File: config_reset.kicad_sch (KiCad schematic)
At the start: 20 parts, among them U1 NX1H35 PBGA625, U6 M95P32-IXMNT/E, Y2 LFSPXO025225_25MHz

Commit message: SDRAM, bank5
last iteration of sdram. max optimization routing and space wise. Traced 2 frams to Bank 5. Fanout of bank 5 for DF9
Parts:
- R1, R14, R19, R3, R31, R32, R6, R7, R8, R9: footprint Resistor_SMD:R_0603_1608Metric_Pad0.98x0.95mm_HandSolder -> Resistor_SMD:R_0402_1005Metric_Pad0.72x0.64mm_HandSolder
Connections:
- no-connect marks 21 -> 94

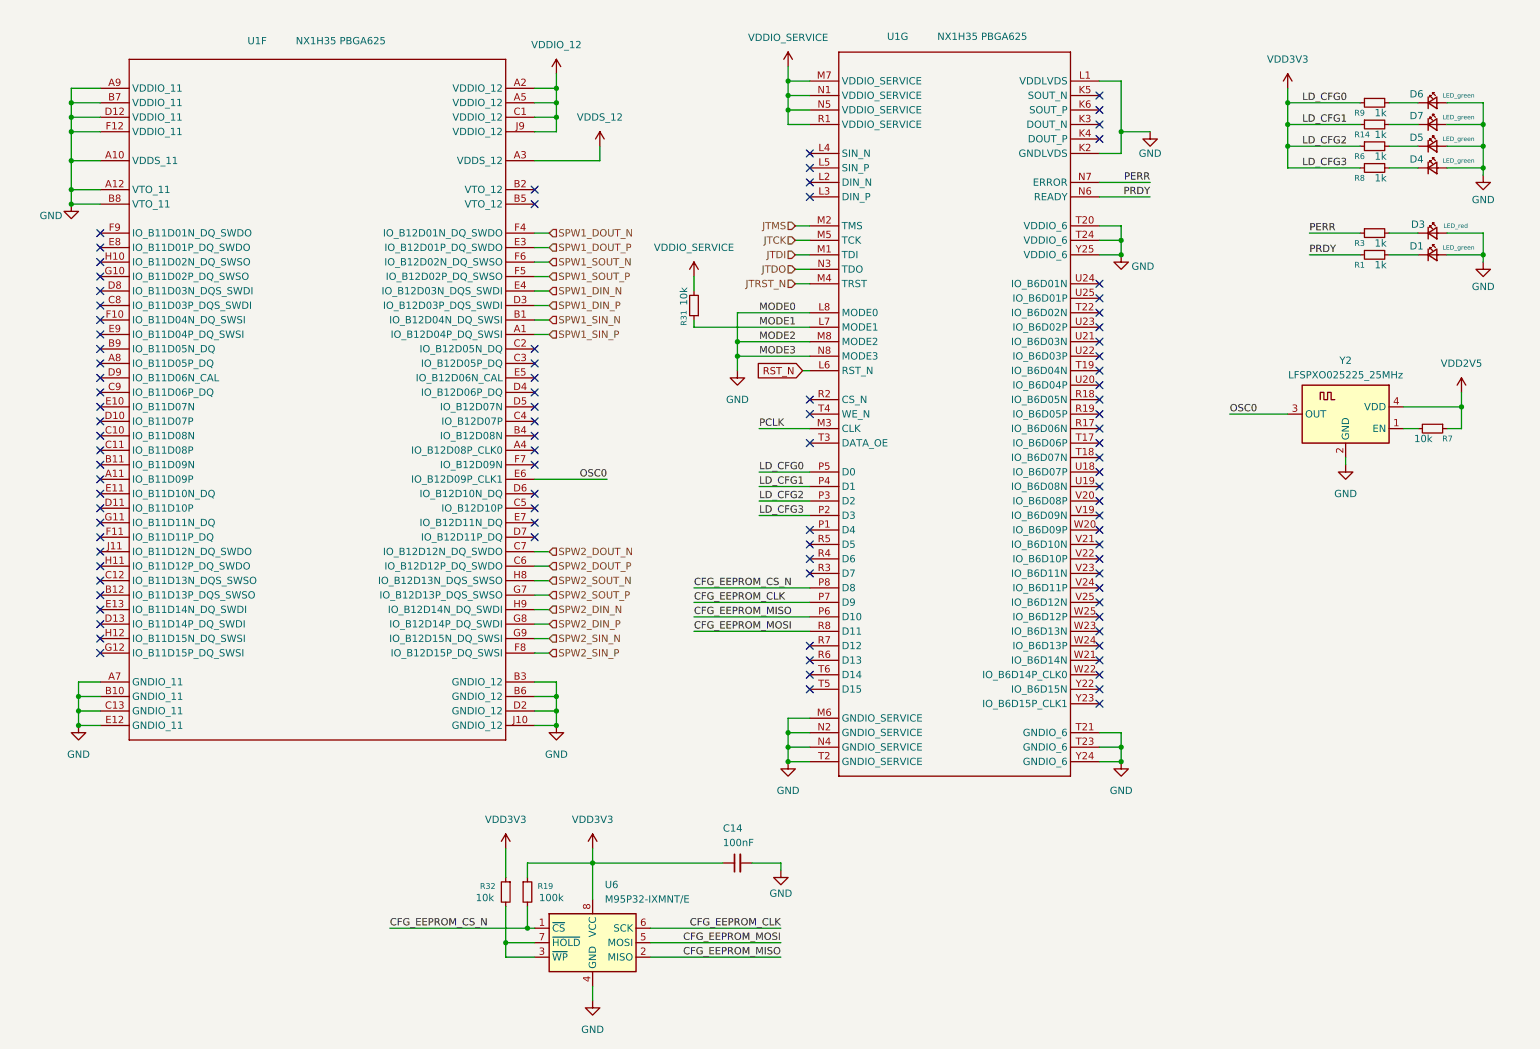
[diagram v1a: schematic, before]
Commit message: added MAX, picoblade, NPN
added the LDO (placement), added the picoblade connector for CFG and deleted one SPW out of 2 in the DF9.
added the NPN transistor (placed)
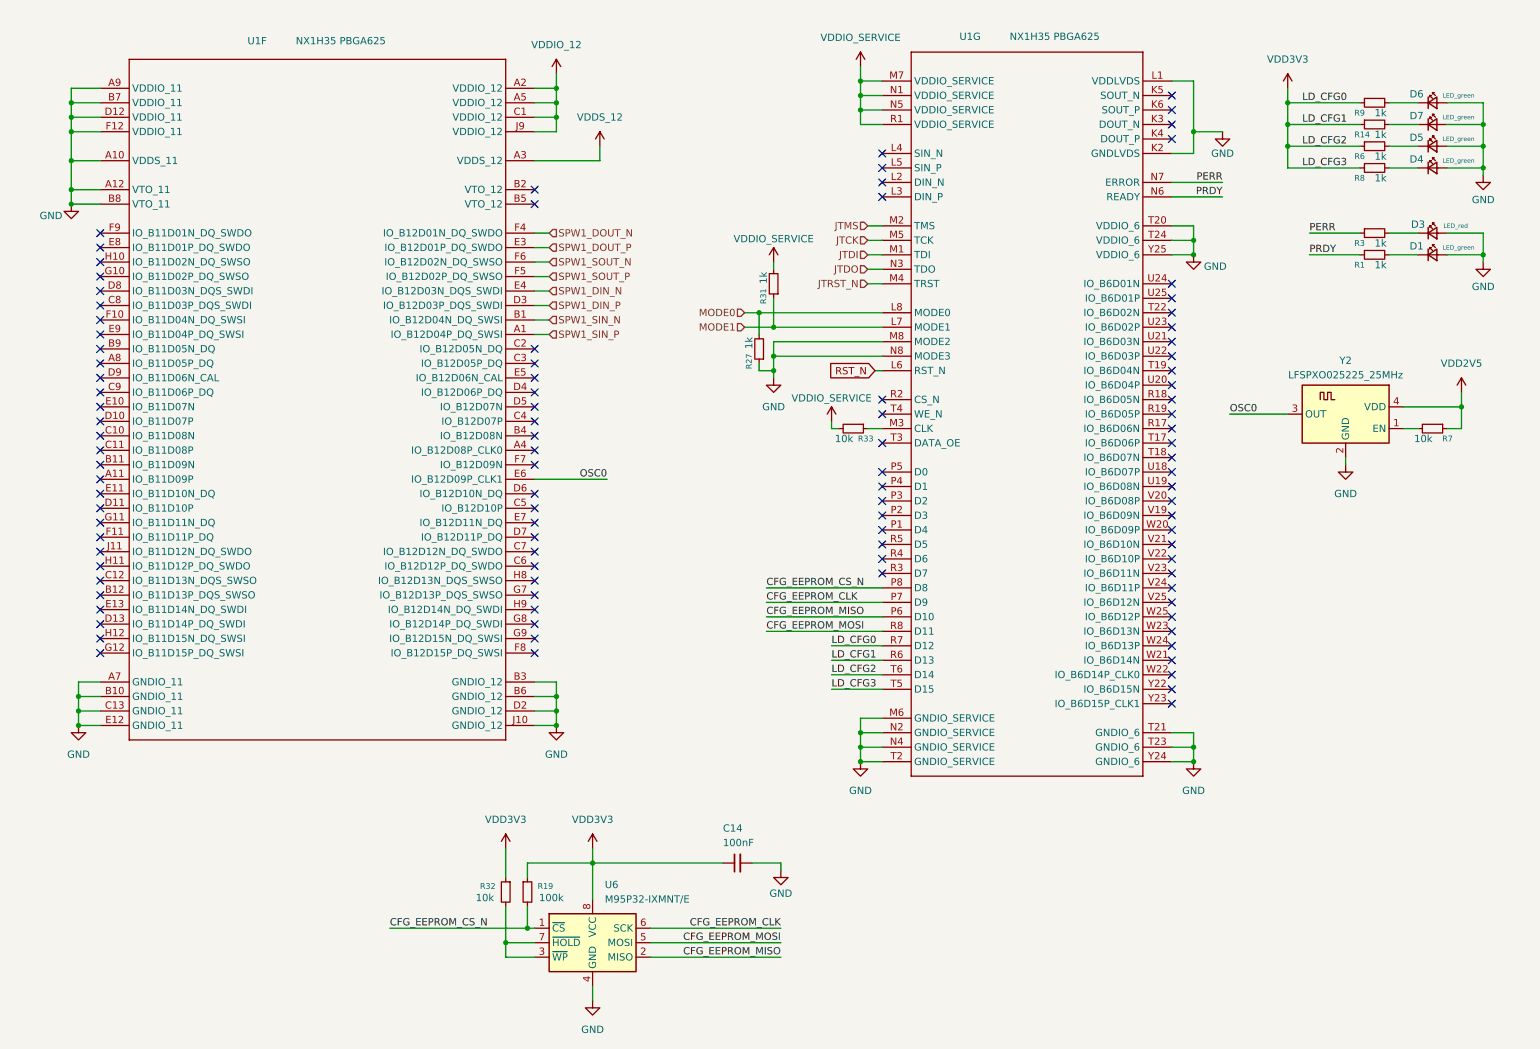
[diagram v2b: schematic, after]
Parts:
- added R27: 1k, Resistor_SMD:R_0402_1005Metric_Pad0.72x0.64mm_HandSolder, symbol Device:R_Small
- added R33: 10k, Resistor_SMD:R_0402_1005Metric_Pad0.72x0.64mm_HandSolder, symbol Device:R_Small
- R31: value 10k -> 1k
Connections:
- net GND: now also R27.1; no longer U1.L8 (MODE0)
- net VDD3V3: now also U1.R6 (D13), U1.R7 (D12), U1.T5 (D15), U1.T6 (D14); no longer U1.P2 (D3), U1.P3 (D2), U1.P4 (D1), U1.P5 (D0)
- net VDDIO_SERVICE: now also R33.2
- net PCLK: no longer names the net of U1.M3 (CLK)
- net PCLK: now also R33.1
- net SPW2_DIN_N: no longer names the net of U1.H9 (IO_B12D14N_DQ_SWDI)
- net SPW2_DIN_P: no longer names the net of U1.G8 (IO_B12D14P_DQ_SWDI)
- net SPW2_DOUT_N: no longer names the net of U1.C7 (IO_B12D12N_DQ_SWDO)
- net SPW2_DOUT_P: no longer names the net of U1.C6 (IO_B12D12P_DQ_SWDO)
- net SPW2_SIN_N: no longer names the net of U1.G9 (IO_B12D15N_DQ_SWSI)
- net SPW2_SIN_P: no longer names the net of U1.F8 (IO_B12D15P_DQ_SWSI)
- net SPW2_SOUT_N: no longer names the net of U1.H8 (IO_B12D13N_DQS_SWSO)
- net SPW2_SOUT_P: no longer names the net of U1.G7 (IO_B12D13P_DQS_SWSO)
- new net MODE0: R27.2, U1.L8 (MODE0)
- no-connect marks 94 -> 102
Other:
- moved on the sheet: U1G

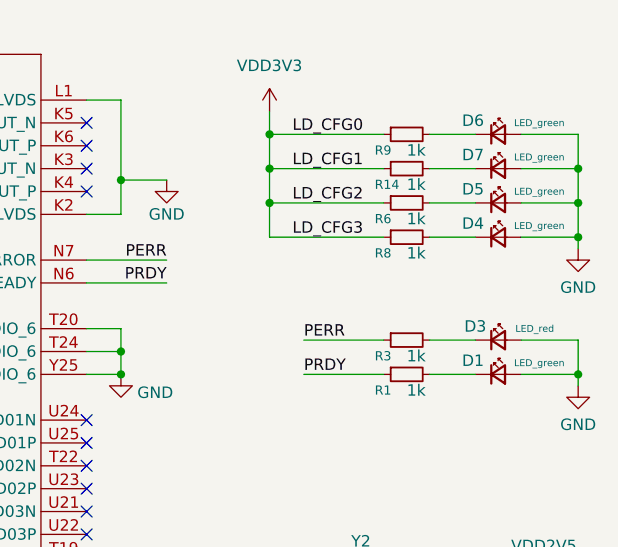
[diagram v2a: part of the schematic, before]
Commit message: full components, LEDS, changed edges
all components on pcb editor. added and  routed leds and 2 PLL. changed edges o have more space
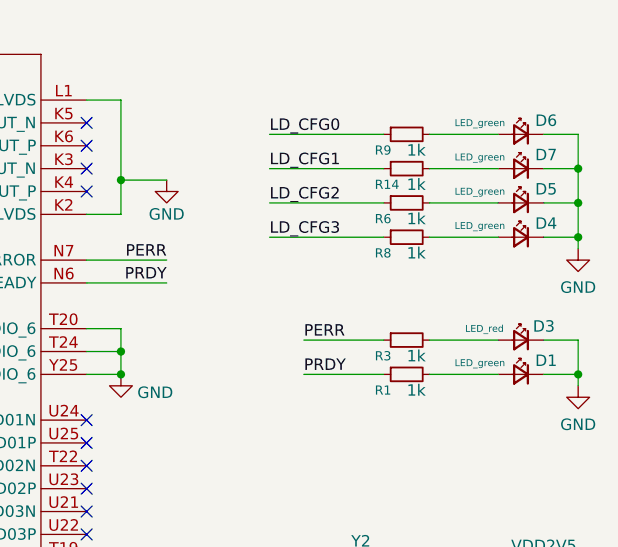
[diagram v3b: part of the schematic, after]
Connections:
- net GND: now also D1.1 (K), D3.1 (K), D4.1 (K), D5.1 (K), D6.1 (K), D7.1 (K); no longer D1.2 (A), D3.2 (A), D4.2 (A), D5.2 (A), D6.2 (A), D7.2 (A)
- net VDD3V3: no longer R14.1, R6.1, R8.1, R9.1, U1.R6 (D13), U1.R7 (D12), U1.T5 (D15), U1.T6 (D14)
- net at R6.2: now also D5.2 (A); no longer D5.1 (K)
- net at R8.2: now also D4.2 (A); no longer D4.1 (K)
- net at R9.2: now also D6.2 (A); no longer D6.1 (K)
- net at R1.2: now also D1.2 (A); no longer D1.1 (K)
- net at R14.2: now also D7.2 (A); no longer D7.1 (K)
- net at R3.2: now also D3.2 (A); no longer D3.1 (K)
- new net LD_CFG0: R9.1, U1.R7 (D12)
- new net LD_CFG1: R14.1, U1.R6 (D13)
- new net LD_CFG2: R6.1, U1.T6 (D14)
- new net LD_CFG3: R8.1, U1.T5 (D15)
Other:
- moved on the sheet: D1, D3, D4, D5, D6, D7

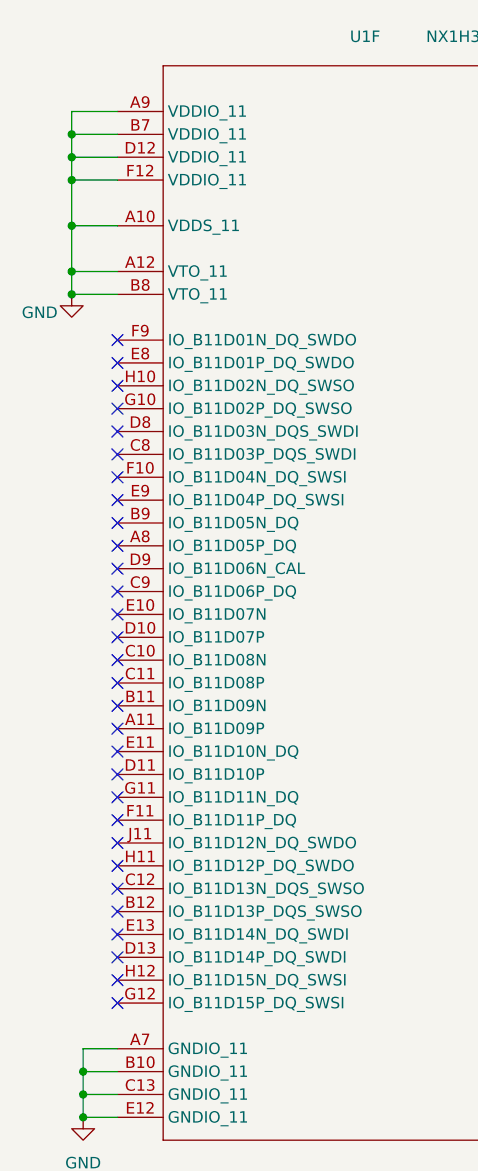
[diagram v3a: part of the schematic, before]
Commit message: SPW Bank0
completed SPW, rotated edges and adjusted dimensions to make the extra sdram bga fit. completed Bank 0 (still to route to connector). Started fanout of bga sdram
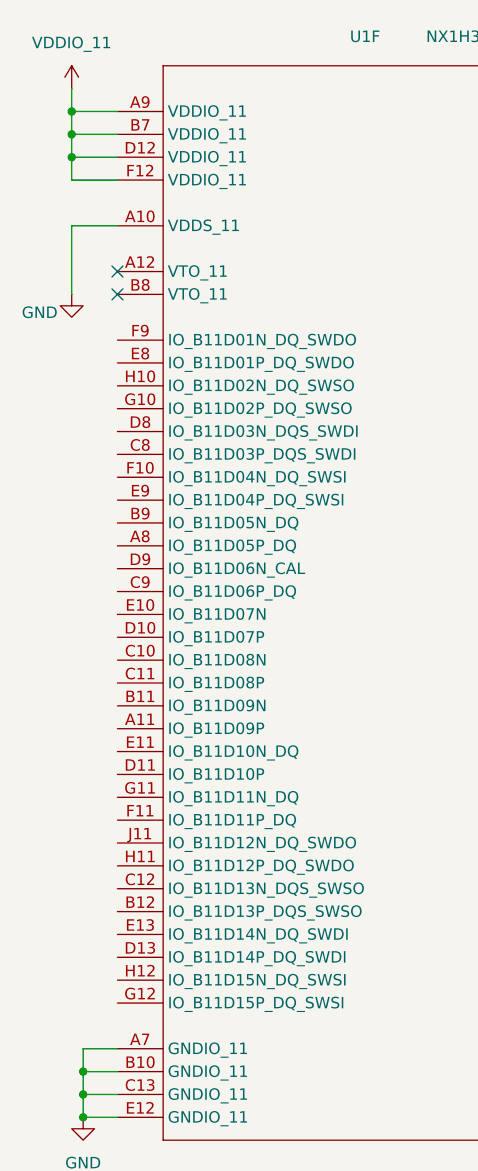
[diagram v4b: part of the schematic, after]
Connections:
- net GND: no longer U1.A12 (VTO_11), U1.A9 (VDDIO_11), U1.B7 (VDDIO_11), U1.B8 (VTO_11), U1.D12 (VDDIO_11), U1.F12 (VDDIO_11)
- new net VDDIO_11: U1.A9 (VDDIO_11), U1.B7 (VDDIO_11), U1.D12 (VDDIO_11), U1.F12 (VDDIO_11)
- no-connect marks 102 -> 74
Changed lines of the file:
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@@
 	(paper "A4")
 	(junction
-		(at 25.4 50.8)
-		(diameter 0)
-		(color 0 0 0 0)
-	)
-	(junction
 		(at 269.24 86.36)
 		(diameter 0)
@@
 	)
 	(junction
-		(at 25.4 38.1)
-		(diameter 0)
-		(color 0 0 0 0)
-	)
-	(junction
 		(at 148.59 77.47)
 		(diameter 0)
@@
 	)
 	(junction
-		(at 25.4 43.18)
+		(at 25.4 30.48)
 		(diameter 0)
 		(color 0 0 0 0)
@@
 	)
 	(junction
-		(at 25.4 48.26)
-		(diameter 0)
-		(color 0 0 0 0)
-	)
-	(junction
 		(at 148.59 72.39)
 		(diameter 0)
@@
 	)
 	(no_connect
-		(at 30.48 119.38)
-	)
-	(no_connect
-		(at 30.48 111.76)
-	)
-	(no_connect
 		(at 218.44 67.31)
 	)
@@
 	)
 	(no_connect
-		(at 30.48 99.06)
-	)
-	(no_connect
 		(at 218.44 31.75)
 	)
@@
 	)
 	(no_connect
-		(at 30.48 83.82)
-	)
-	(no_connect
-		(at 30.48 73.66)
-	)
-	(no_connect
 		(at 218.44 135.89)
 	)
@@
 	)
 	(no_connect
-		(at 30.48 58.42)
-	)
-	(no_connect
 		(at 218.44 118.11)
 	)
@@
 	)
 	(no_connect
-		(at 30.48 63.5)
-	)
-	(no_connect
 		(at 106.68 86.36)
 	)
@@
 	)
 	(no_connect
-		(at 30.48 55.88)
-	)
-	(no_connect
-		(at 30.48 127)
+		(at 30.48 48.26)
 	)
 	(no_connect
@@
 	)
 	(no_connect
-		(at 30.48 81.28)
-	)
-	(no_connect
 		(at 106.68 121.92)
 	)
@@
 	)
 	(no_connect
-		(at 30.48 78.74)
-	)
-	(no_connect
 		(at 106.68 109.22)
 	)
@@
 	)
 	(no_connect
-		(at 30.48 124.46)
-	)
-	(no_connect
 		(at 106.68 116.84)
 	)
 	(no_connect
-		(at 30.48 71.12)
-	)
-	(no_connect
 		(at 167.64 97.79)
 	)
 	(no_connect
-		(at 30.48 121.92)
-	)
-	(no_connect
 		(at 218.44 64.77)
 	)
@@
 	)
 	(no_connect
-		(at 30.48 60.96)
-	)
-	(no_connect
 		(at 218.44 34.29)
 	)
@@
 	)
 	(no_connect
-		(at 30.48 116.84)
-	)
-	(no_connect
 		(at 167.64 115.57)
 	)
 	(no_connect
-		(at 30.48 66.04)
+		(at 106.68 106.68)
 	)
 	(no_connect
-		(at 106.68 106.68)
+		(at 30.48 50.8)
 	)
 	(no_connect
@@
 	)
 	(no_connect
-		(at 30.48 106.68)
-	)
-	(no_connect
-		(at 30.48 68.58)
-	)
-	(no_connect
 		(at 167.64 100.33)
 	)
@@
 	)
 	(no_connect
-		(at 30.48 91.44)
-	)
-	(no_connect
-		(at 30.48 104.14)
-	)
-	(no_connect
 		(at 167.64 41.91)
 	)
@@
 	)
 	(no_connect
-		(at 30.48 88.9)
-	)
-	(no_connect
 		(at 218.44 128.27)
 	)
@@
 	)
 	(no_connect
-		(at 30.48 109.22)
-	)
-	(no_connect
-		(at 30.48 96.52)
-	)
-	(no_connect
 		(at 167.64 87.63)
 	)
@@
 	)
 	(no_connect
-		(at 30.48 86.36)
-	)
-	(no_connect
 		(at 167.64 44.45)
 	)
@@
 	)
 	(no_connect
-		(at 30.48 76.2)
-	)
-	(no_connect
 		(at 218.44 130.81)
 	)
@@
 	)
 	(no_connect
-		(at 30.48 114.3)
-	)
-	(no_connect
 		(at 218.44 125.73)
 	)
 	(no_connect
-		(at 30.48 129.54)
-	)
-	(no_connect
 		(at 218.44 100.33)
 	)
@@
 		(at 106.68 50.8)
 	)
-	(no_connect
-		(at 30.48 93.98)
-	)
-	(no_connect
-		(at 30.48 101.6)
-	)
 	(wire
 		(pts
@@
 	(wire
 		(pts
+			(xy 25.4 27.94) (xy 25.4 30.48)
+		)
+		(stroke
+			(width 0)
+			(type default)
+		)
+	)
+	(wire
+		(pts
 			(xy 106.68 66.04) (xy 109.22 66.04)
 		)
@@
 	(wire
 		(pts
-			(xy 25.4 43.18) (xy 25.4 48.26)
+			(xy 25.4 43.18) (xy 25.4 50.8)
 		)
 		(stroke
@@
 	(wire
 		(pts
-			(xy 25.4 38.1) (xy 25.4 43.18)
-		)
-		(stroke
-			(width 0)
-			(type default)
-		)
-	)
-	(wire
-		(pts
 			(xy 106.68 71.12) (xy 109.22 71.12)
 		)
@@
 	(wire
 		(pts
-			(xy 30.48 48.26) (xy 25.4 48.26)
-		)
-		(stroke
-			(width 0)
-			(type default)
-		)
-	)
-	(wire
-		(pts
 			(xy 163.83 146.05) (xy 163.83 148.59)
 		)
@@
 	(wire
 		(pts
-			(xy 25.4 48.26) (xy 25.4 50.8)
-		)
-		(stroke
-			(width 0)
-			(type default)
-		)
-	)
-	(wire
-		(pts
 			(xy 149.86 166.37) (xy 149.86 167.64)
 		)
@@
 	(wire
 		(pts
-			(xy 25.4 50.8) (xy 30.48 50.8)
-		)
-		(stroke
-			(width 0)
-			(type default)
-		)
-	)
-	(wire
-		(pts
 			(xy 163.83 34.29) (xy 163.83 36.83)
 		)
@@
 					(unit 1)
 				)
+			)
+		)
+	)
+	(symbol
+		(lib_id "DataHub_PWR_symbols:VDDIO_11")
+		(at 25.4 27.94 0)
+		(unit 1)
+		(exclude_from_sim no)
+		(in_bom yes)
+		(on_board yes)
+		(dnp no)
+		(fields_autoplaced yes)
+		(property "Reference" "#PWR051"
+			(at 9.398 22.86 0)
+			(effects
+				(font
+					(size 1.27 1.27)
+				)
+				(hide yes)
+			)
+		)
+		(property "Value" "VDDIO_11"
+			(at 25.4 22.86 0)
+			(effects
+				(font
+					(size 1.27 1.27)
+				)
+			)
+		)
+		(property "Footprint" ""
+			(at 25.4 27.94 0)
+			(effects
+				(font
+					(size 1.27 1.27)
+				)
+				(hide yes)
+			)
+		)
+		(property "Datasheet" ""
+			(at 25.4 27.94 0)
+			(effects
+				(font
+					(size 1.27 1.27)
+				)
+				(hide yes)
+			)
+		)
+		(property "Description" "Power symbol creates a global label with name \"VDDIO_11\""
+			(at 23.368 18.542 0)
+			(effects
+				(font
+					(size 1.27 1.27)
+				)
+				(hide yes)
+			)
+		)
+		(pin "1"
+		)
+		(instances
+			(project ""
+				(path "/ae14ff2f-b8e3-4dd1-9329-e73906805e39/e4b4090a-9491-4976-8b45-759656425e5b"
+					(reference "#PWR051")
+					(unit 1)
+				)
